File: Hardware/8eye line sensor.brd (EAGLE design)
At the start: 203.2 x 76.2 mm, 64 parts, among them U101 QRE1113, U102 QRE1113, U103 QRE1113, U104 QRE1113, U105 QRE1113, U106 QRE1113, U107 QRE1113, U108 QRE1113, U8 PCF8575C

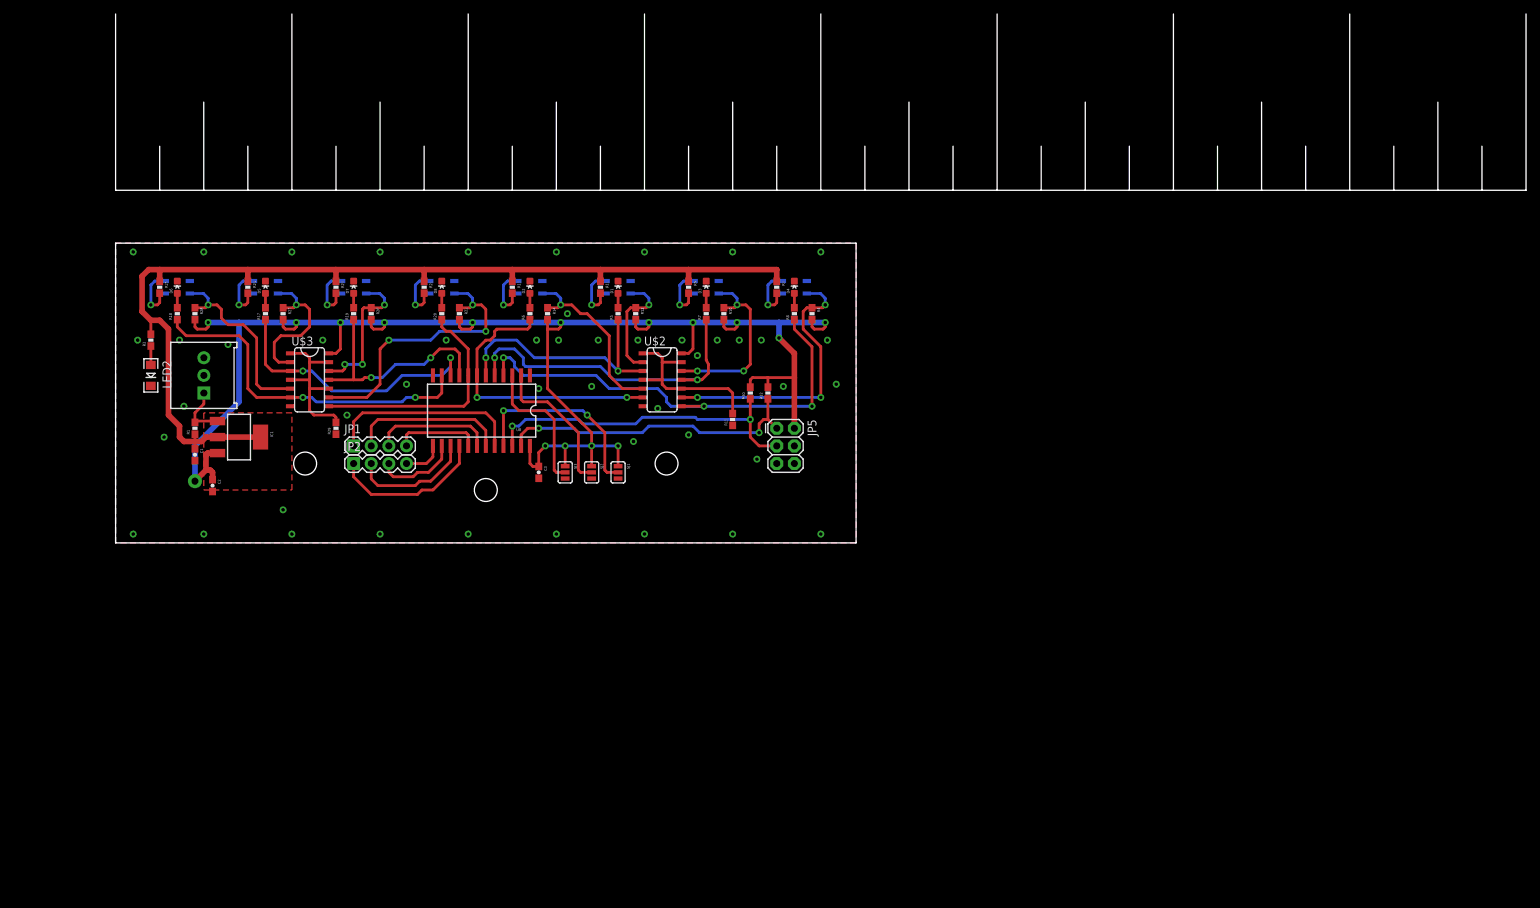
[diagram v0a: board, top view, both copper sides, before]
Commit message: Shrunk PCB
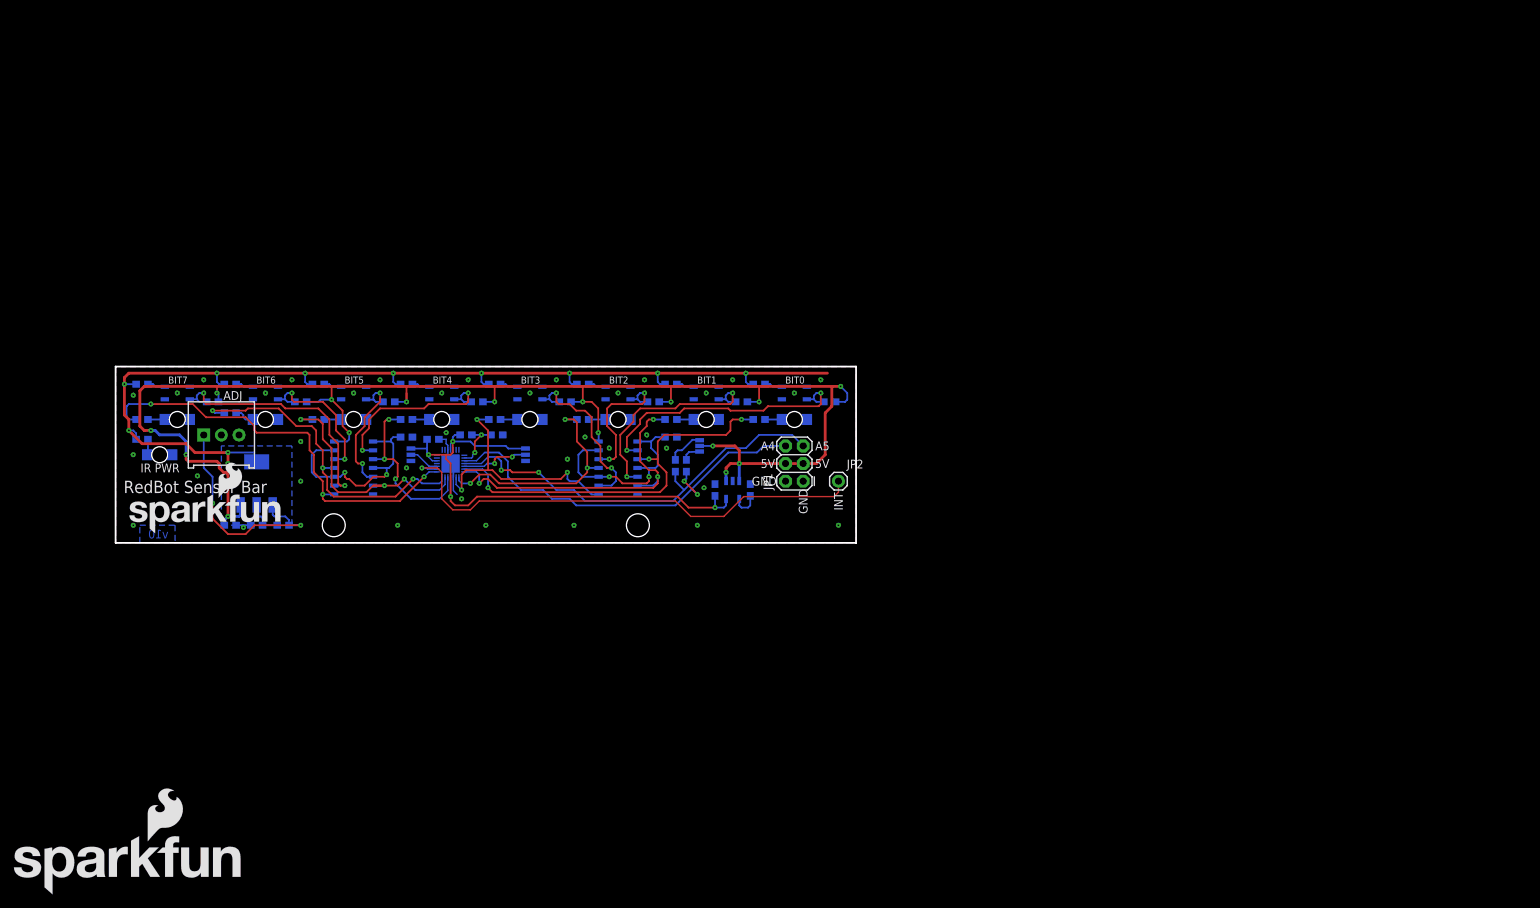
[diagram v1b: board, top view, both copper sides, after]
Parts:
- removed IC1: (no value), SparkFun-PowerIC:SOT223
- removed JP5: AVR_SPI_PRG_6PTH, SparkFun-Connectors:2X3
- removed U$2, U$3: 74ACT125D, SparkFun-Retired:SO014
- removed U8: PCF8575C, SparkFun:SO-24DW
- added C4: 2.2uF, SparkFun-Capacitors:0603-CAP
- added C5, C6: 470pF, SparkFun-Capacitors:0603-CAP
- added FRAME2: FRAME-LEDGER, SparkFun-Aesthetics:CREATIVE_COMMONS
- added LOGO1: SFE_LOGO_NAME_FLAME.3_INCH, SparkFun-Aesthetics:SFE_LOGO_NAME_FLAME_.3
- added R31: 100, SparkFun-Passives:0603-RES
- added U1: SX1509, SparkFun-DigitalIC:QFN-28
- added U2, U4: 74ACT125D, SparkFun-Retired:SO014
- added U3: 3.3V/150mA, SparkFun-PowerIC:SOT23-5
- added U5: LM1117, SparkFun-PowerIC:SOT223
- D1, D2, D3, D4, D5, D6, D7, D8: value GREEN -> Green; device SparkFun-LED:LED-0603 -> SparkFun-LED:LED-1206-BOTTOM
- JP1: value (none) -> FEMALE 2x3; device SparkFun-Connectors:1X04 -> SparkFun-Connectors:2X3
- JP2: value (none) -> INT; device SparkFun-Connectors:1X04 -> SparkFun-Connectors:1X01
- LED2: value Power -> Green; device SparkFun-Nate:LED-1206 -> SparkFun-LED:LED-1206-BOTTOM
- R1: value (none) -> 4.7K
- R10, R12, R14, R22, R26, R27, R28, R4: value (none) -> 68K
- R11, R13, R21, R23, R24, R25, R3, R9: value (none) -> 100
- R15, R29, R30, R32: value (none) -> 10K
- R17, R18, R19, R20, R5, R6, R7, R8: value (none) -> 1K
- SJ3: value A2 -> A1; device SparkFun:SJ_3 -> SparkFun-Passives:PAD-JUMPER-3-NC_BY_PASTE_YES_SILK_FULL_BOX
- U$1: device SparkFun-Electromechanical:STAND-OFF -> SparkFun-Aesthetics:SFE_LOGO_NAME_FLAME_.2
- moved JP2 69.9 mm to (104.1, 8.89)
- moved JP1 65.0 mm to (99.1, 8.89), turned to 90 degrees
- moved U$1 52.5 mm to (1.27, 1.27)
- moved R20 45.8 mm to (3.81, 17.8), flipped to the bottom, turned to 180 degrees
- moved R8 45.8 mm to (54.6, 17.8), flipped to the bottom, turned to 180 degrees
- moved D4 42.6 mm to (59.7, 17.8), flipped to the bottom, turned to 180 degrees
- moved D8 42.6 mm to (8.89, 17.8), flipped to the bottom, turned to 180 degrees
- moved D1 31.8 mm to (97.8, 17.8), flipped to the bottom, turned to 180 degrees
- moved D2 31.8 mm to (85.1, 17.8), flipped to the bottom, turned to 180 degrees
- moved D6 31.8 mm to (34.3, 17.8), flipped to the bottom, turned to 180 degrees
- moved D5 31.7 mm to (47.0, 17.8), flipped to the bottom, turned to 180 degrees
- moved SJ2 26.2 mm to (42.5, 12.7), flipped to the bottom
- moved R6 25.4 mm to (80.0, 17.8), flipped to the bottom, turned to 180 degrees
- moved R17 25.4 mm to (41.9, 17.8), flipped to the bottom, turned to 180 degrees
- moved R18 25.4 mm to (29.2, 17.8), flipped to the bottom, turned to 180 degrees
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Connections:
- removed net A2: SJ3.2, U8.3
- removed net P10: JP2.4, U8.13
- removed net P11: JP2.3, U8.14
- removed net P12: JP2.2, U8.15
- removed net P13: JP2.1, U8.16
- removed net P14: JP1.4, U8.17
- removed net P15: JP1.3, U8.18
- removed net P16: JP1.2, U8.19
- removed net P17: JP1.1, U8.20
- new net I2C_PWR: C3.1, C4.1, R31.1, SJ1.1, SJ2.1, U1.12, U1.18, U1.4, U3.5
- new net N$4: R30.2, SJ3.1
- new net N$6: C5.1, U3.4
- new net N$8: R32.2, SJ3.3
- new net ~RESET: C6.1, R31.2, U1.23
- net !ENBLSB: now also U2.1, U2.10, U2.13, U2.4; no longer U$2.1, U$2.10, U$2.13, U$2.4
- net !ENBMSB: now also U4.1, U4.10, U4.13, U4.4; no longer U$3.1, U$3.10, U$3.13, U$3.4
- net A0: now also U1.26; no longer U8.21
- net A1: now also U1.10; no longer U8.2
- net GND: now also C4.2, C5.2, C6.2, JP1.1, JP1.2, U1.17, U1.29, U1.3, U2.7, U3.2, U4.7; no longer JP5.6, SJ3.3, U$2.7, U$3.7, U8.12
- net INT: now also JP2.1, U1.9; no longer U8.1
- net LED_BIAS: now also U5.2, U5.4; no longer IC1.2, IC1.4
- net N$1: now also U5.1; no longer IC1.1
- net SCL: now also JP1.5, U1.25; no longer JP5.3, U8.22
- net SDA: now also JP1.6, U1.24; no longer JP5.1, U8.23
- net SEN1: now also U2.2; no longer U$2.9
- net SEN1BUF: now also R5.1, U1.27, U2.3; no longer R8.1, U$2.8, U8.4
- net SEN2: now also U2.5; no longer U$2.12
- net SEN2BUF: now also R6.1, U1.28, U2.6; no longer R7.1, U$2.11, U8.5
- net SEN3: now also U2.12; no longer U$2.2
- net SEN3BUF: now also R7.1, U1.1, U2.11; no longer R5.1, U$2.3, U8.6
- net SEN4: now also U2.9; no longer U$2.5
- net SEN4BUF: now also R8.1, U1.2, U2.8; no longer R6.1, U$2.6, U8.7
- net SEN5: now also U4.2; no longer U$3.9
- net SEN5BUF: now also R17.1, U1.5, U4.3; no longer R20.1, U$3.8, U8.8
- net SEN6: now also U4.5; no longer U$3.12
- net SEN6BUF: now also R18.1, U1.6, U4.6; no longer R19.1, U$3.11, U8.9
- net SEN7: now also U4.12; no longer U$3.2
- net SEN7BUF: now also R19.1, U1.7, U4.11; no longer R17.1, U$3.3, U8.10
- net SEN8: now also U4.9; no longer U$3.5
- net SEN8BUF: now also R20.1, U1.8, U4.8; no longer R18.1, U$3.6, U8.11
- net VCC: now also JP1.3, JP1.4, SJ3.2, U2.14, U3.1, U3.3, U4.14, U5.3; no longer C3.1, IC1.3, JP5.2, R30.2, R32.2, SJ1.1, SJ2.1, SJ3.1, U$2.14, U$3.14, U8.24
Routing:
- net I2C_PWR: track 0.00 -> 79.3 mm, vias 0 -> 4
- net INT: track 0.00 -> 71.4 mm, vias 0 -> 1
- net P17: track 28.4 -> 0.00 mm
- net N$1: track 8.09 -> 33.6 mm, vias 0 -> 2
- net P16: track 22.6 -> 0.00 mm
- net P13: track 22.6 -> 0.00 mm
- net A2: track 20.1 -> 0.00 mm
- net A0: track 28.4 -> 9.88 mm
- net P12: track 17.7 -> 0.00 mm
- net P15: track 17.3 -> 0.00 mm
- net A1: track 21.2 -> 4.43 mm
- net SDA: track 44.9 -> 60.1 mm
- net VCC: track 236.3 -> 221.6 mm
- net SEN5: track 41.3 -> 27.3 mm, vias 3 -> 2
- net P14: track 12.3 -> 0.00 mm
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- added copper zone on layer 16, net LED_BIAS
- removed copper zone on layer 1, net LED_BIAS
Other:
- board size 203.2 x 76.2 mm -> 106.7 x 25.4 mm
- board text added: "5V"
- board text added: "A4"
- board text added: "A5"
- board text added: "ADJ"
- board text added: "BIT0"
- board text added: "BIT1"
- board text added: "BIT2"
- board text added: "BIT3"
- board text added: "BIT4"
- board text added: "BIT5"
- board text added: "BIT6"
- board text added: "BIT7"
- board text added: "GND"
- board text added: "INT"
- board text added: "IR PWR"
- board text added: "RedBot Sensor Bar"
- board text added: "v10"

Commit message: logos and 47 measures and t_place added, Oh my!
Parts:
- removed LOGO1: SFE_LOGO_NAME_FLAME.3_INCH, SparkFun-Aesthetics:SFE_LOGO_NAME_FLAME_.3
- removed U$1: (no value), SparkFun-Aesthetics:SFE_LOGO_NAME_FLAME_.2
- added FID1, FID2: FIDUCIALUFIDUCIAL, SparkFun-Aesthetics:MICRO-FIDUCIAL
- added LOGO2, LOGO4: SFE_LOGO_NAME.2_INCH, SparkFun-Aesthetics:SFE_LOGO_NAME_.2
- added LOGO3, LOGO5: SFE_LOGO_FLAME.3_INCH, SparkFun-Aesthetics:SFE_LOGO_FLAME_.3
- added LOGO6: OSHW-LOGOS, SparkFun-Aesthetics:OSHW-LOGO-S
- STANDOFF1, STANDOFF2: value (none) -> STAND-OFF
- renumbered U$4 to STANDOFF2, U$5 to STANDOFF1
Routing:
- net SDA: track 60.1 -> 61.4 mm
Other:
- board text added: "0"
- board text added: "1"
- board text added: "Dimentions from axis"
- board text added: "Dimentions from origin"
- board text added: "I2C A0"
- board text added: "I2C A1"
- board text added: "I2C PULL"
- board text added: "Units in inches"
- board text added: "v02"
- board text removed: "v10"

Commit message: about ready for proto submit
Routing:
- net LED_BIAS: track 158.6 -> 146.8 mm
- net SEN7BUF: track 48.0 -> 49.5 mm
- net SDA: track 61.4 -> 60.2 mm
- net SEN6BUF: track 37.3 -> 38.5 mm
- net SEN1: track 39.8 -> 38.9 mm
- net N$1: track 33.6 -> 34.5 mm
- net GND: vias 37 -> 44
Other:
- board text added: "A0"
- board text added: "A1"
- board text added: "I2C"
- board text removed: "I2C A0"
- board text removed: "I2C A1"

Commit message: fixed for QC
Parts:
- added STANDOFF3, STANDOFF4: STAND-OFF, SparkFun-Electromechanical:STAND-OFF
- R1, R11, R13, R15, R17, R18, R19, R20, R21, R23, R24, R25, R29, R3, R30, R31, R32, R5, R6, R7, R8, R9: device SparkFun-Passives:0603-RES -> SparkFun-Resistors:0603-RES
- R10, R12, R14, R22, R26, R27, R28, R4: device SparkFun-Passives:0603-RES -> SparkFun-Resistors:0603
- R16: value TRIMPOT-PTH-KNOB -> TSR-3386
- R2: value 330 -> 33OHM; device SparkFun:0603-RES -> SparkFun-Resistors:0603
- U2, U4: value 74ACT125D -> IC-08880
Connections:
- removed net SEN8: R28.1, U108.3, U4.9
- removed net SEN8BUF: R20.1, U1.8, U4.8
- new net SEN0: R4.1, U101.3, U2.2
- new net SEN0BUF: R5.1, U1.27, U2.3
- net SEN1: now also R10.1, U102.3, U2.5; no longer R4.1, U101.3, U2.2
- net SEN1BUF: now also R6.1, U1.28, U2.6; no longer R5.1, U1.27, U2.3
- net SEN2: now also R12.1, U103.3, U2.12; no longer R10.1, U102.3, U2.5
- net SEN2BUF: now also R7.1, U1.1, U2.11; no longer R6.1, U1.28, U2.6
- net SEN3: now also R14.1, U104.3, U2.9; no longer R12.1, U103.3, U2.12
- net SEN3BUF: now also R8.1, U1.2, U2.8; no longer R7.1, U1.1, U2.11
- net SEN4: now also R22.1, U105.3, U4.2; no longer R14.1, U104.3, U2.9
- net SEN4BUF: now also R17.1, U1.5, U4.3; no longer R8.1, U1.2, U2.8
- net SEN5: now also R26.1, U106.3, U4.5; no longer R22.1, U105.3, U4.2
- net SEN5BUF: now also R18.1, U1.6, U4.6; no longer R17.1, U1.5, U4.3
- net SEN6: now also R27.1, U107.3, U4.12; no longer R26.1, U106.3, U4.5
- net SEN6BUF: now also R19.1, U1.7, U4.11; no longer R18.1, U1.6, U4.6
- net SEN7: now also R28.1, U108.3, U4.9; no longer R27.1, U107.3, U4.12
- net SEN7BUF: now also R20.1, U1.8, U4.8; no longer R19.1, U1.7, U4.11
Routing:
- net SEN8BUF: track 62.0 -> 0.00 mm, vias 3 -> 0
- net SEN0BUF: track 0.00 -> 57.6 mm, vias 0 -> 3
- net SEN0: track 0.00 -> 38.9 mm, vias 0 -> 2
- net SEN8: track 37.0 -> 0.00 mm, vias 2 -> 0
- net SEN7: track 20.9 -> 35.5 mm
- net SEN2BUF: track 47.8 -> 33.9 mm
- net SEN5BUF: track 25.5 -> 38.5 mm
- net SEN7BUF: track 49.5 -> 62.0 mm
- net SEN4BUF: track 36.8 -> 25.5 mm
- net SEN6BUF: track 38.5 -> 49.5 mm
- net SEN2: track 32.2 -> 21.5 mm
- net SEN1BUF: track 57.6 -> 47.8 mm
- net SEN5: track 27.1 -> 19.7 mm
- net SEN1: track 38.9 -> 32.2 mm
- net SEN3: track 21.5 -> 25.3 mm
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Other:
- board text added: "(+)"
- board text added: "(-)"
- board text added: "2"
- board text added: "3"
- board text added: "4"
- board text added: "5"
- board text added: "6"
- board text added: "7"
- board text added: "Marshall Taylor"
- board text added: "USE IC-08880 FOR U2 AND U4-- FOOTPRINT WILL BE UPDATED LATER"
- board text removed: "BIT0"
- board text removed: "BIT1"
- board text removed: "BIT2"
- board text removed: "BIT3"
- board text removed: "BIT4"
- board text removed: "BIT5"
- board text removed: "BIT6"
- board text removed: "BIT7"

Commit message: fixed half the issues
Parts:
- removed U4: IC-08880, SparkFun-Retired:SO014
- added C7: 2.2uF, SparkFun-Capacitors:0603-CAP
- added SJ5: JUMPER-PAD-3-2OF3_NC_BY_TRACE_SMALL, SparkFun-Passives:PAD-JUMPER-3-2OF3_NC_BY_TRACE_YES_SILK_FULL_BOX
- added U6: 74AC125, SparkFun-DigitalIC:SO14
- SJ1, SJ2: device SparkFun:SJ_3 -> SparkFun-Passives:PAD-JUMPER-3-2OF3_NC_BY_PASTE_YES_SILK_FULL_BOX
- SJ3: device SparkFun-Passives:PAD-JUMPER-3-NC_BY_PASTE_YES_SILK_FULL_BOX -> SparkFun-Passives:PAD-JUMPER-3-3OF3_NC_BY_TRACE_YES_SILK_FULL_BOX
- U2: value IC-08880 -> 74AC125; device SparkFun-Retired:SO014 -> SparkFun-DigitalIC:SO14
- moved C4 1.42 mm to (87.6, 6.99)
- moved C5 1.27 mm to (92.7, 7.62)
- moved U3 1.27 mm to (90.2, 7.62)
- moved SJ3 0.93 mm to (84.6, 13.2), flipped to the top, turned to 90 degrees
- moved U2 0.63 mm to (72.4, 10.8)
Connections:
- new net N$19: SJ3.2, SJ5.2
- net !ENBMSB: now also U6.1, U6.10, U6.13, U6.4; no longer U4.1, U4.10, U4.13, U4.4
- net GND: now also C7.2, U6.7; no longer U4.7
- net I2C_PWR: now also C7.1, SJ5.3; no longer U1.4
- net SEN4: now also U6.2; no longer U4.2
- net SEN4BUF: now also U6.3; no longer U4.3
- net SEN5: now also U6.5; no longer U4.5
- net SEN5BUF: now also U6.6; no longer U4.6
- net SEN6: now also U6.12; no longer U4.12
- net SEN6BUF: now also U6.11; no longer U4.11
- net SEN7: now also U6.9; no longer U4.9
- net SEN7BUF: now also U6.8; no longer U4.8
- net VCC: now also SJ5.1, U1.4, U6.14; no longer SJ3.2, U4.14
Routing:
- net VCC: track 221.0 -> 236.4 mm, vias 16 -> 17
- net I2C_PWR: track 79.7 -> 85.7 mm, vias 4 -> 3
- net N$19: track 0.00 -> 4.10 mm
- net SEN5BUF: track 38.5 -> 36.9 mm
- net SEN7: track 35.5 -> 37.0 mm
- net SEN6: track 20.9 -> 19.4 mm
- net N$8: track 2.83 -> 4.12 mm, vias 0 -> 1
- net N$4: track 5.28 -> 5.52 mm, vias 0 -> 1
- net GND: vias 46 -> 50
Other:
- board text added: "v03"
- board text removed: "v02"

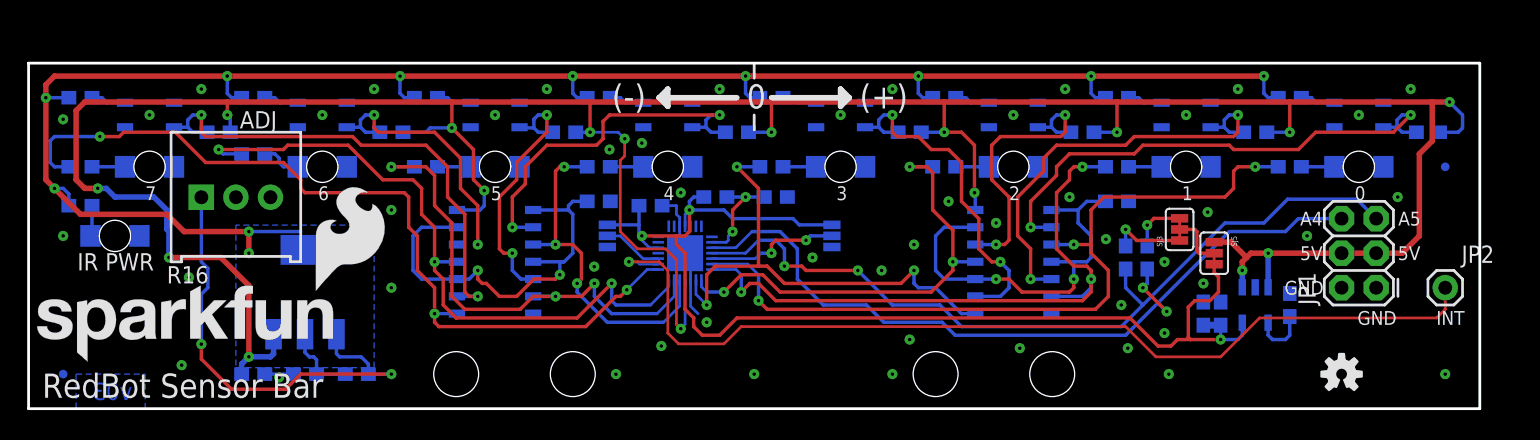
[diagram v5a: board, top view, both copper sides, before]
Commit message: Ran DRC, fixing aesthetic
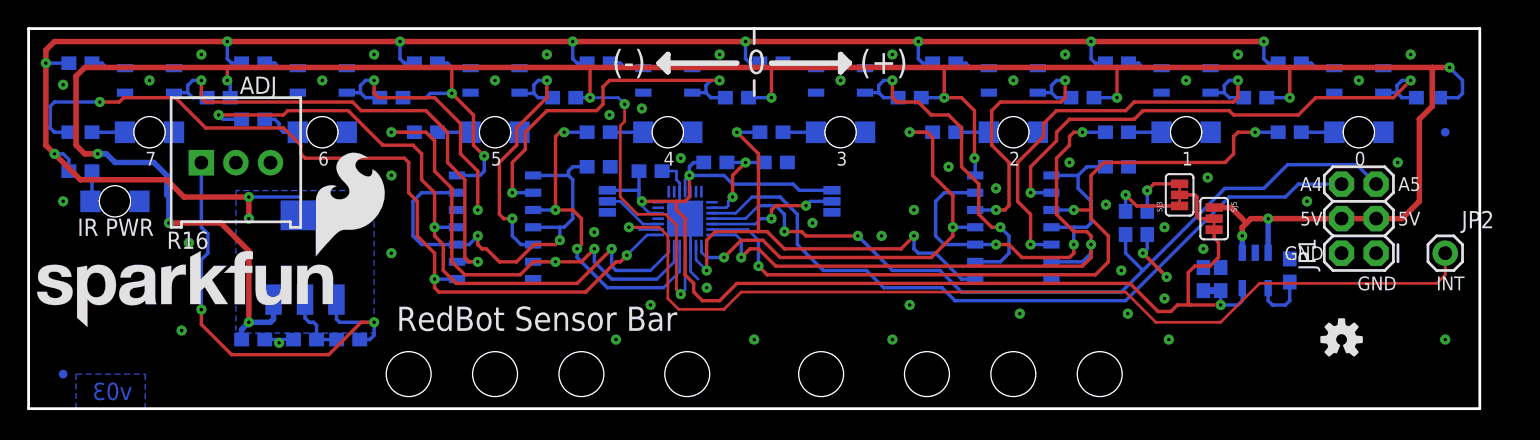
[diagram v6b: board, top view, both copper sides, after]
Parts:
- added STANDOFF5, STANDOFF6, STANDOFF7, STANDOFF8: STAND-OFF, SparkFun-Electromechanical:STAND-OFF
- moved STANDOFF1 3.49 mm to (27.9, 2.54)
- moved STANDOFF2 3.49 mm to (78.7, 2.54)
- moved R1 2.62 mm to (23.5, 5.08)
- moved C6 2.54 mm to (54.9, 18.1)
- moved LED2 2.54 mm to (6.35, 15.2)
- moved R15 2.54 mm to (80.0, 17.8)
- moved R16 2.54 mm to (15.2, 18.1)
- moved R29 2.54 mm to (41.9, 17.8)
- moved R31 2.54 mm to (50.5, 18.1)
- moved SJ1 2.54 mm to (59.1, 15.2)
- moved SJ2 2.54 mm to (42.5, 15.2)
- moved SJ3 2.54 mm to (84.6, 15.7)
- moved SJ5 2.54 mm to (87.2, 14.0)
- moved U1 2.54 mm to (48.3, 14.0)
- moved U2 2.54 mm to (72.4, 13.3)
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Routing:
- net N$1: track 34.5 -> 33.3 mm
- net LED_BIAS: track 146.8 -> 146.2 mm
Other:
- board size 106.7 x 25.4 mm -> 106.7 x 27.9 mm
- board text added: "Units in inches unless specified"
- board text added: "mils"
- board text removed: "USE IC-08880 FOR U2 AND U4-- FOOTPRINT WILL BE UPDATED LATER"
- board text removed: "Units in inches"

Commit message: ready for review of prototype 2 (v03)
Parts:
- added R33, R34: 4.7K, SparkFun-Resistors:0603-RES
- moved R29 14.0 mm to (27.9, 18.4), turned to 180 degrees
- moved LOGO2 6.20 mm to (64.5, 3.64)
- moved SJ5 1.75 mm to (87.2, 15.7)
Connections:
- new net N$10: R34.2, SJ2.1
- new net N$21: R33.2, SJ1.1
- net I2C_PWR: now also R33.1, R34.1; no longer SJ1.1, SJ2.1
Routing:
- net N$21: track 0.00 -> 3.55 mm
- net N$10: track 0.00 -> 3.38 mm
- net I2C_PWR: track 85.7 -> 82.6 mm
- net VCC: track 236.4 -> 238.9 mm
- net N$19: track 4.10 -> 2.54 mm
- net !ENBMSB: track 31.0 -> 32.6 mm
- net SEN6: track 19.4 -> 20.9 mm
- net GND: vias 50 -> 51
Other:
- board text added: "3.3V"
- board text added: "b0"
- board text added: "b1"
- board text added: "b2"
- board text added: "b3"
- board text added: "b4"
- board text added: "b5"
- board text added: "b6"
- board text added: "b7"
- board text removed: "2"
- board text removed: "3"
- board text removed: "4"
- board text removed: "5"
- board text removed: "6"
- board text removed: "7"
